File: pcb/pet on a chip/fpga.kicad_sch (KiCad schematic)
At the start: 28 parts, among them J3 Conn_02x15_Odd_Even, J4 Conn_02x15_Odd_Even, SW1 SW_Push, SW2 SW_Push, U5 N25Q032A13ESC40F, U6 ICE40HX8K-BG121, U7 L77HDE15SD1CH4F, X2 ASTX-H11

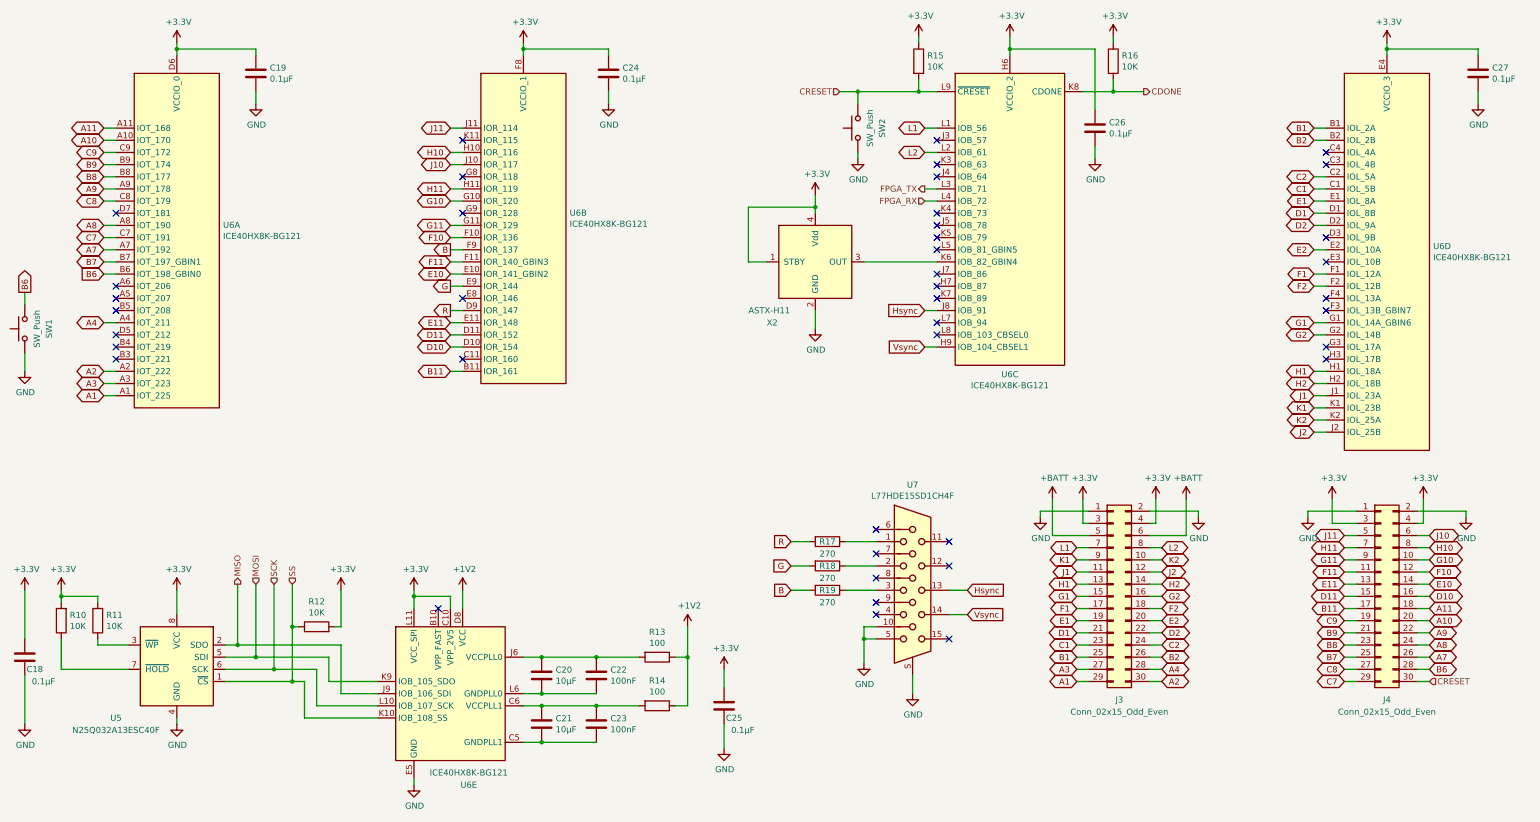
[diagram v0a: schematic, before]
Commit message: updated to kicad 8
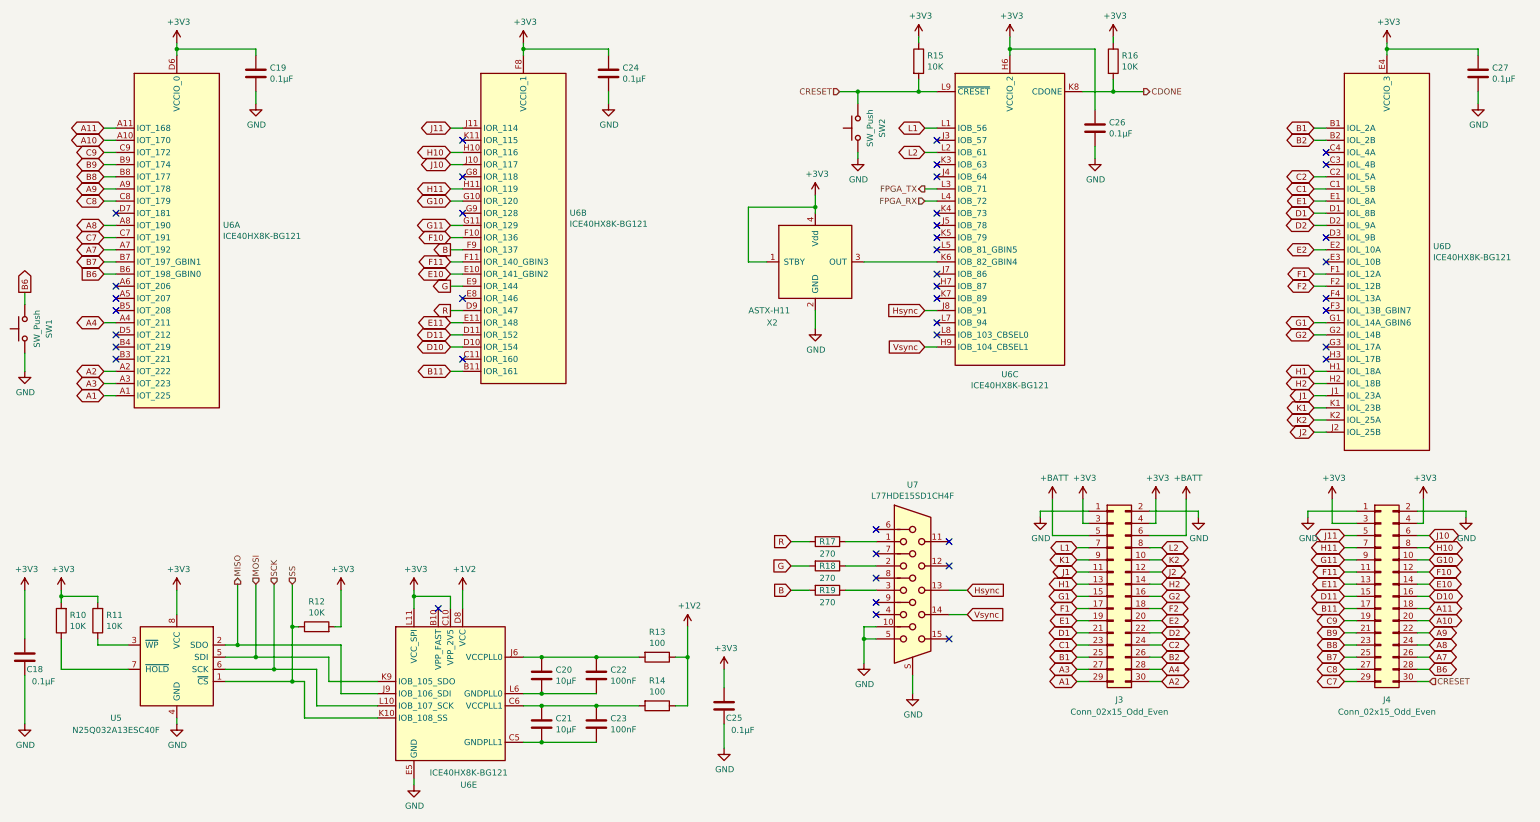
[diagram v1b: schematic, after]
